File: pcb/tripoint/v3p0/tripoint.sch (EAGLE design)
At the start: 54 parts, among them J1 TC2030-JLINK-NL, J2 TC2030-JLINK-NL, T1 HHM1595A1, U1 STM32F091CC, U2 DW1000, U3 SKY13317, U4 LXDC2HN18A, X1 38.4M, X2 16M

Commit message: added LED, test pads, external signals and Lab11 power symbols
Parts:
- removed J1: TC2030-JLINK-NL, connector:TC2030-JLINK-NL
- added D1: SML-LX0404SIUPGUSB, leds:SML-LX0404SIUPGUSB
- added R5, R6, R7: 1k, passives:RESISTOR0402_RES
- added TP1, TP2: TEST_POINT_0.040IN, headers:TEST_POINT_0.040IN
- added TP3, TP4: TEST-POINT, headers:TEST-POINT
- R1, R2, R3, R4: device rcl:R-EU_R0201 -> passives:RESISTOR0201_RES
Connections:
- net I2C1_SCL renamed EXT_I2C_SCL
- net I2C1_SDA renamed EXT_I2C_SDA
- net SPI_CLK renamed DW_SPI_CLK
- net V1P8 renamed 1V8
- net V1P8_EN renamed REG_EN
- net V3P3 renamed 3V3
- removed net !SPI1_SS: U1.PA4
- removed net !SPI_CS: U2.!SPICS
- removed net GPIO4: J1.VCC, U1.PB10
- removed net GPIO5: J1.GND, U1.PB11
- removed net SPI1_MISO: U1.PA6
- removed net SPI1_MOSI: U1.PA7
- removed net SPI_MISO: U2.SPIMISO
- removed net SPI_MOSI: U2.SPIMOSI
- new net !DW_SPI_CS: U1.PA4, U2.!SPICS
- new net DW_SPI_MISO: U1.PA6, U2.SPIMISO
- new net DW_SPI_MOSI: U1.PA7, U2.SPIMOSI
- new net LED_BLUE: R7.2, U1.PB12
- new net LED_GREEN: R6.2, U1.PB13
- new net LED_RED: R5.2, U1.PB14
- new net N$10: D1.G, R6.1
- new net N$11: D1.B, R7.1
- new net N$12: D1.R, R5.1
- net +3V3: now also D1.VDD
- net GPIO0: now also TP1.TESTPOINT; no longer J1.!RESET
- net GPIO1: now also TP2.TESTPOINT; no longer J1.SWO
- net GPIO2: now also TP3.TESTPOINT, U1.PB10; no longer J1.SWDCLK, U1.PB8
- net GPIO3: now also TP4.TESTPOINT, U1.PB11; no longer J1.SWDIO, U1.PB9
- net INTERRUPT: now also U1.PA2; no longer U1.PA3
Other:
- note added: "EXTERNAL SIGNALS"
- note added: "I2C: Pull-up resistor required"
- note added: "INTERRUPT: used both for waking up from STOP (USART2_TX) and STANDBY (WKUP4)"
- note added: "LED"
- note added: "Note: Additional I2C pull-up resistors required"
- note added: "PC Test Points"
- note added: "Pad Test Points"
- note added: "The following signals must be integrated into all designs using the design block:"

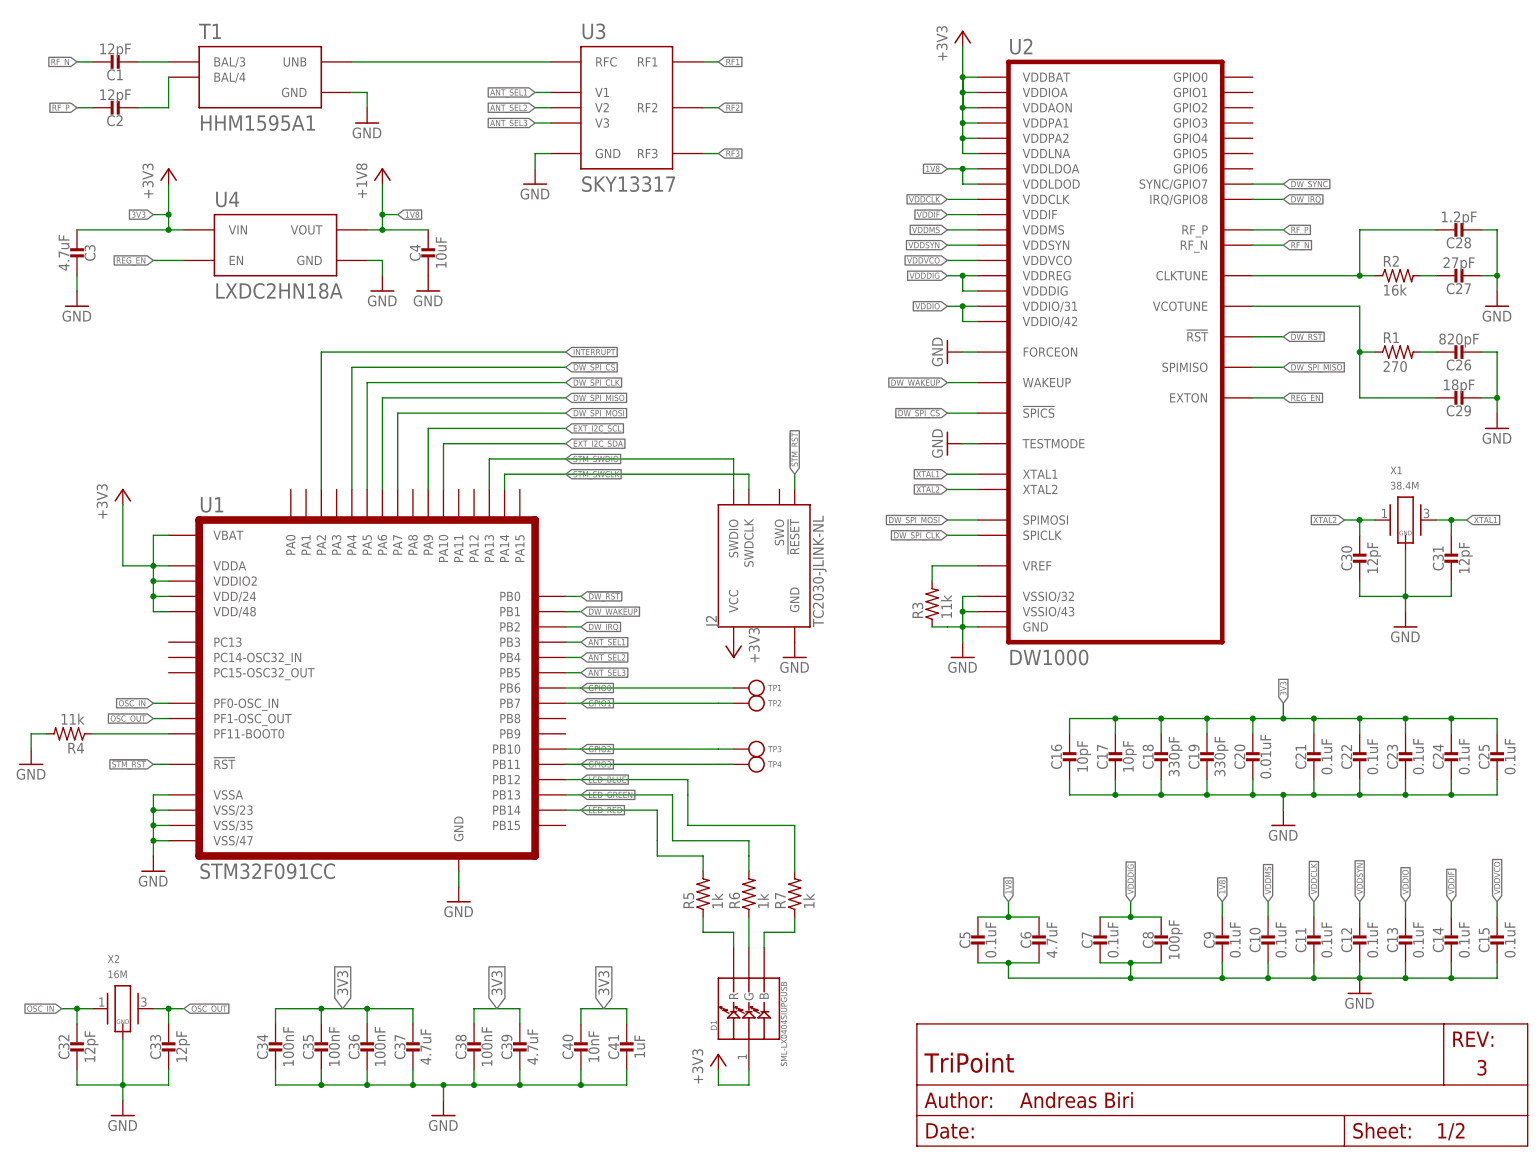
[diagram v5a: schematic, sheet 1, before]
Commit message: corrected decoupling cap values, added correct res for DEEPSLEEP plus missing decoupling caps
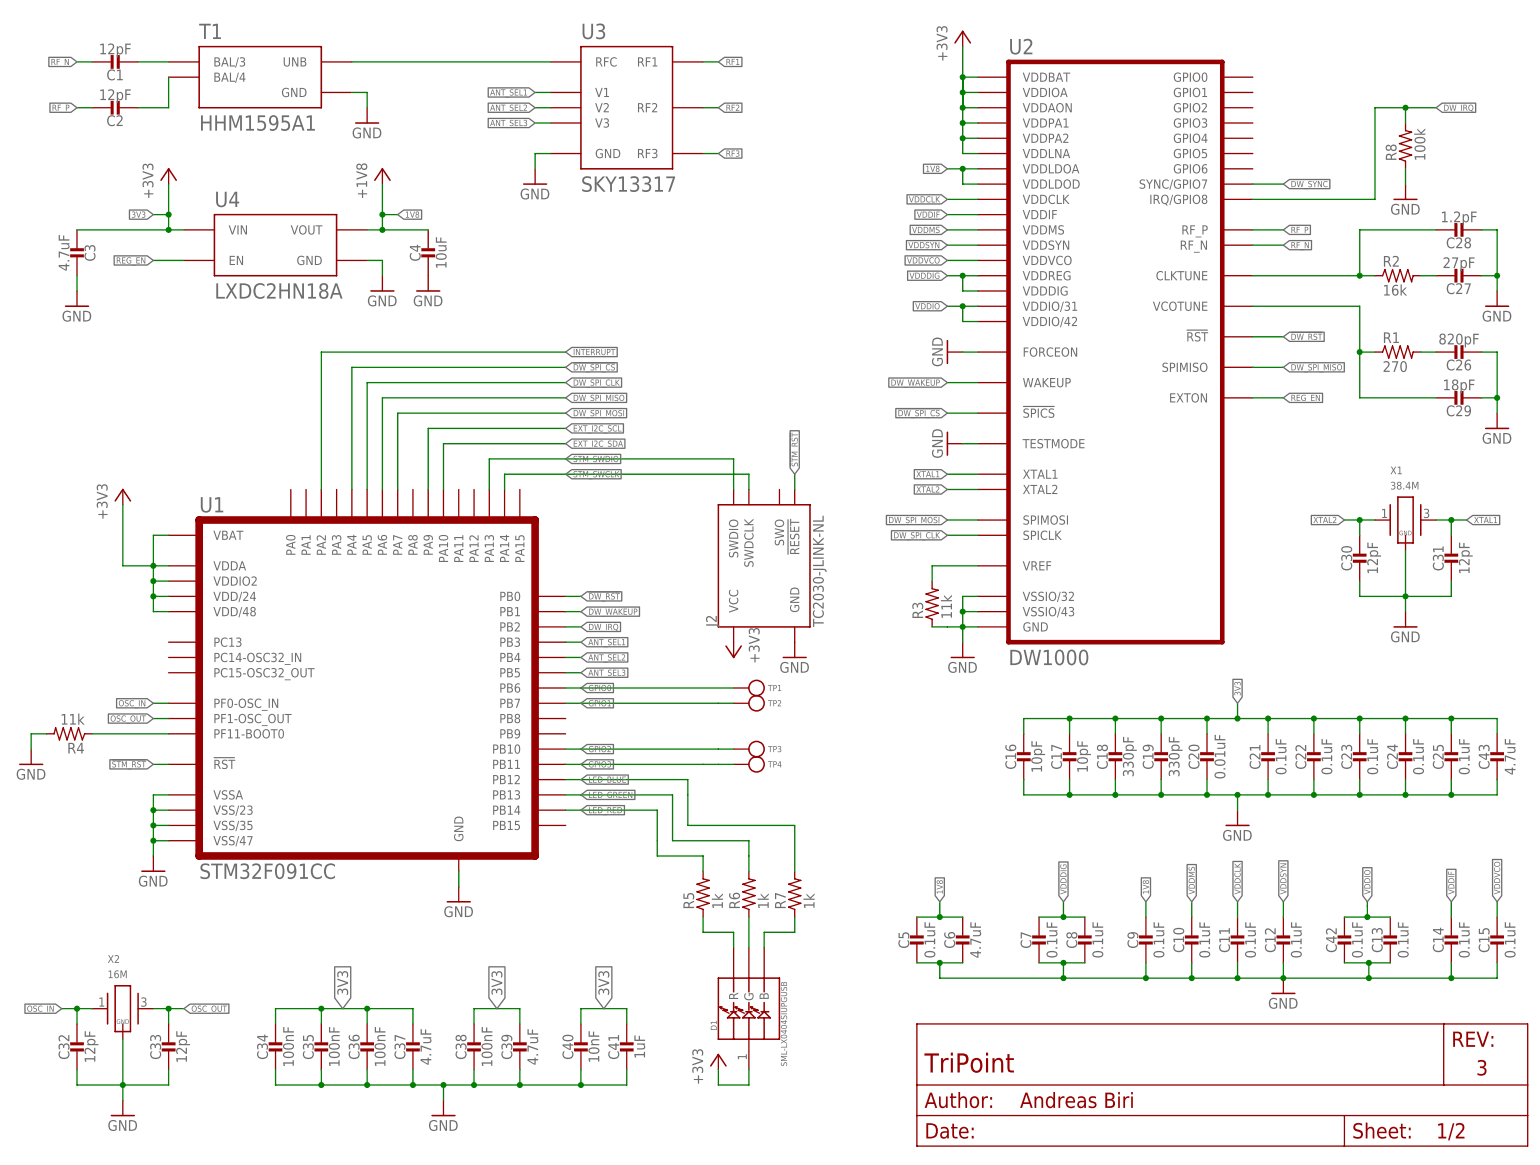
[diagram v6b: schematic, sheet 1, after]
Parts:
- added C42: 0.1uF, passives:CAPACITOR0201_CAP
- added C43: 4.7uF, passives:CAPACITOR0603_CAP
- added R8: 100k, passives:RESISTOR0201_RES
- C8: value 100pF -> 0.1uF
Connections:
- net 3V3: now also C43.1
- net DW_IRQ: now also R8.2
- net GND: now also C42.2, C43.2, R8.1
- net VDDIO: now also C42.1
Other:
- note added: "Pull-down for (DEEP)SLEEP"
- moved on the sheet: C10, C11, C12, C13, C16, C17, C18, C19, C20, C21, C22, C23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

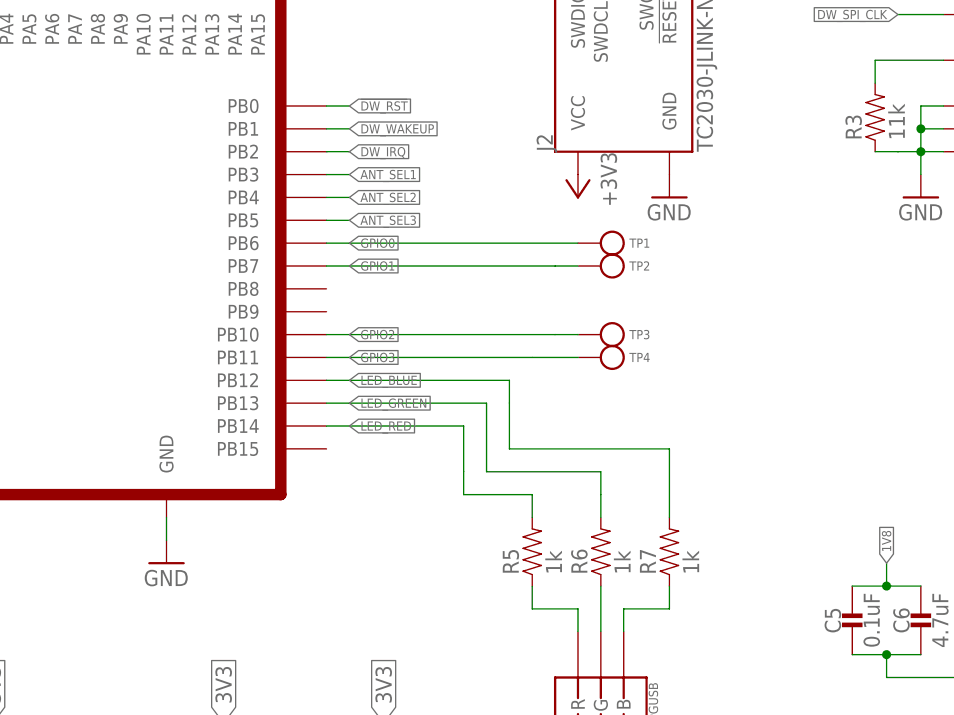
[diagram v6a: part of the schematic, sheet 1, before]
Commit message: completed layout, optimized pin positioning for module
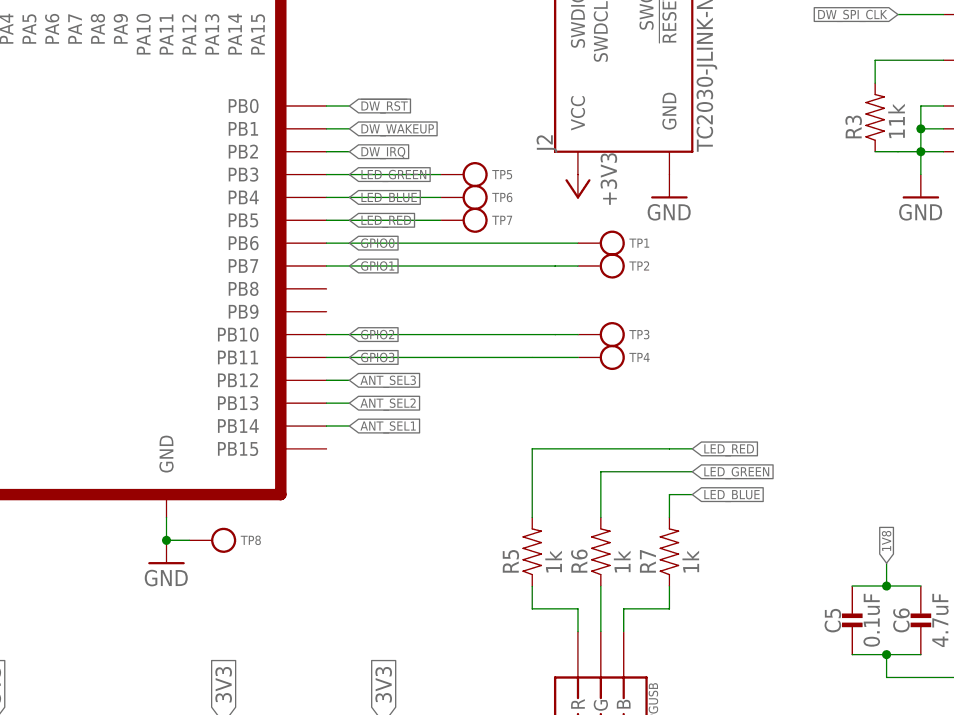
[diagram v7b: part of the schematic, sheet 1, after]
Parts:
- added TP5, TP6, TP7, TP8: TEST-POINT, headers:TEST-POINT
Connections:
- net ANT_SEL1: now also U1.PB14; no longer U1.PB3
- net ANT_SEL2: now also U1.PB13; no longer U1.PB4
- net ANT_SEL3: now also U1.PB12; no longer U1.PB5
- net GND: now also TP8.TESTPOINT
- net LED_BLUE: now also TP6.TESTPOINT, U1.PB4; no longer U1.PB12
- net LED_GREEN: now also TP5.TESTPOINT, U1.PB3; no longer U1.PB13
- net LED_RED: now also TP7.TESTPOINT, U1.PB5; no longer U1.PB14
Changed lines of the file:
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@@
 <part name="C42" library="passives" deviceset="CAPACITOR" device="0201_CAP" value="0.1uF"/>
 <part name="C43" library="passives" deviceset="CAPACITOR" device="0603_CAP" value="4.7uF"/>
+<part name="TP5" library="headers" deviceset="TEST-POINT" device=""/>
+<part name="TP6" library="headers" deviceset="TEST-POINT" device=""/>
+<part name="TP7" library="headers" deviceset="TEST-POINT" device=""/>
+<part name="TP8" library="headers" deviceset="TEST-POINT" device=""/>
 </parts>
 <sheets>
@@
 <instance part="C42" gate="G$1" x="223.52" y="35.56"/>
 <instance part="C43" gate="G$1" x="248.92" y="66.04"/>
+<instance part="TP5" gate="G$1" x="109.22" y="83.82" rot="R180"/>
+<instance part="TP6" gate="G$1" x="109.22" y="81.28" rot="R180"/>
+<instance part="TP7" gate="G$1" x="109.22" y="78.74" rot="R180"/>
+<instance part="TP8" gate="G$1" x="81.28" y="43.18" rot="R180"/>
 </instances>
 <busses>
@@
 <wire x1="76.2" y1="45.72" x2="76.2" y2="43.18" width="0.1524" layer="91"/>
 <pinref part="SUPPLY9" gate="G1" pin="GND"/>
+<pinref part="TP8" gate="G$1" pin="TESTPOINT"/>
+<wire x1="76.2" y1="43.18" x2="78.74" y2="43.18" width="0.1524" layer="91"/>
+<junction x="76.2" y="43.18"/>
 </segment>
 <segment>
@@
 </segment>
 <segment>
-<pinref part="U1" gate="U1" pin="PB3"/>
-<wire x1="93.98" y1="83.82" x2="96.52" y2="83.82" width="0.1524" layer="91"/>
-<label x="96.52" y="83.82" size="1.016" layer="95" xref="yes"/>
+<label x="96.52" y="55.88" size="1.016" layer="95" xref="yes"/>
+<pinref part="U1" gate="U1" pin="PB14"/>
+<wire x1="96.52" y1="55.88" x2="93.98" y2="55.88" width="0.1524" layer="91"/>
 </segment>
 </net>
@@
 </segment>
 <segment>
-<pinref part="U1" gate="U1" pin="PB4"/>
-<wire x1="93.98" y1="81.28" x2="96.52" y2="81.28" width="0.1524" layer="91"/>
-<label x="96.52" y="81.28" size="1.016" layer="95" xref="yes"/>
+<label x="96.52" y="58.42" size="1.016" layer="95" xref="yes"/>
+<pinref part="U1" gate="U1" pin="PB13"/>
+<wire x1="96.52" y1="58.42" x2="93.98" y2="58.42" width="0.1524" layer="91"/>
 </segment>
 </net>
@@
 </segment>
 <segment>
-<pinref part="U1" gate="U1" pin="PB5"/>
-<wire x1="93.98" y1="78.74" x2="96.52" y2="78.74" width="0.1524" layer="91"/>
-<label x="96.52" y="78.74" size="1.016" layer="95" xref="yes"/>
+<pinref part="U1" gate="U1" pin="PB12"/>
+<wire x1="96.52" y1="60.96" x2="93.98" y2="60.96" width="0.1524" layer="91"/>
+<label x="96.52" y="60.96" size="1.016" layer="95" xref="yes"/>
 </segment>
 </net>
@@
 </segment>
 </net>
-<net name="LED_BLUE" class="0">
-<segment>
-<label x="96.52" y="60.96" size="1.016" layer="95" xref="yes"/>
-<wire x1="96.52" y1="60.96" x2="114.3" y2="60.96" width="0.1524" layer="91"/>
-<wire x1="114.3" y1="60.96" x2="114.3" y2="58.42" width="0.1524" layer="91"/>
-<wire x1="114.3" y1="58.42" x2="114.3" y2="53.34" width="0.1524" layer="91"/>
-<wire x1="114.3" y1="53.34" x2="132.08" y2="53.34" width="0.1524" layer="91"/>
-<pinref part="R7" gate="G$1" pin="2"/>
-<wire x1="132.08" y1="53.34" x2="132.08" y2="45.72" width="0.1524" layer="91"/>
-<pinref part="U1" gate="U1" pin="PB12"/>
-<wire x1="96.52" y1="60.96" x2="93.98" y2="60.96" width="0.1524" layer="91"/>
-</segment>
-</net>
-<net name="LED_GREEN" class="0">
-<segment>
-<label x="96.52" y="58.42" size="1.016" layer="95" xref="yes"/>
-<wire x1="96.52" y1="58.42" x2="111.76" y2="58.42" width="0.1524" layer="91"/>
-<wire x1="111.76" y1="58.42" x2="111.76" y2="50.8" width="0.1524" layer="91"/>
-<wire x1="111.76" y1="50.8" x2="124.46" y2="50.8" width="0.1524" layer="91"/>
-<pinref part="R6" gate="G$1" pin="2"/>
-<wire x1="124.46" y1="48.26" x2="124.46" y2="45.72" width="0.1524" layer="91"/>
-<wire x1="124.46" y1="50.8" x2="124.46" y2="48.26" width="0.1524" layer="91"/>
-<pinref part="U1" gate="U1" pin="PB13"/>
-<wire x1="96.52" y1="58.42" x2="93.98" y2="58.42" width="0.1524" layer="91"/>
-</segment>
-</net>
 <net name="INTERRUPT" class="0">
 <segment>
@@
 <pinref part="U1" gate="U1" pin="PA2"/>
 <wire x1="53.34" y1="109.22" x2="53.34" y2="132.08" width="0.1524" layer="91"/>
-</segment>
-</net>
-<net name="LED_RED" class="0">
-<segment>
-<label x="96.52" y="55.88" size="1.016" layer="95" xref="yes"/>
-<pinref part="R5" gate="G$1" pin="2"/>
-<wire x1="116.84" y1="48.26" x2="116.84" y2="45.72" width="0.1524" layer="91"/>
-<wire x1="116.84" y1="48.26" x2="109.22" y2="48.26" width="0.1524" layer="91"/>
-<wire x1="109.22" y1="48.26" x2="109.22" y2="50.8" width="0.1524" layer="91"/>
-<wire x1="109.22" y1="50.8" x2="109.22" y2="55.88" width="0.1524" layer="91"/>
-<pinref part="U1" gate="U1" pin="PB14"/>
-<wire x1="96.52" y1="55.88" x2="93.98" y2="55.88" width="0.1524" layer="91"/>
-<wire x1="109.22" y1="55.88" x2="96.52" y2="55.88" width="0.1524" layer="91"/>
 </segment>
 </net>
@@
 </segment>
 </net>
+<net name="LED_RED" class="0">
+<segment>
+<pinref part="R5" gate="G$1" pin="2"/>
+<wire x1="116.84" y1="45.72" x2="116.84" y2="53.34" width="0.1524" layer="91"/>
+<wire x1="116.84" y1="53.34" x2="132.08" y2="53.34" width="0.1524" layer="91"/>
+<wire x1="132.08" y1="53.34" x2="134.62" y2="53.34" width="0.1524" layer="91"/>
+<label x="134.62" y="53.34" size="1.016" layer="95" xref="yes"/>
+</segment>
+<segment>
+<pinref part="U1" gate="U1" pin="PB5"/>
+<wire x1="93.98" y1="78.74" x2="96.52" y2="78.74" width="0.1524" layer="91"/>
+<label x="96.52" y="78.74" size="1.016" layer="95" xref="yes"/>
+<pinref part="TP7" gate="G$1" pin="TESTPOINT"/>
+<wire x1="96.52" y1="78.74" x2="106.68" y2="78.74" width="0.1524" layer="91"/>
+</segment>
+</net>
+<net name="LED_BLUE" class="0">
+<segment>
+<pinref part="R7" gate="G$1" pin="2"/>
+<wire x1="132.08" y1="45.72" x2="132.08" y2="48.26" width="0.1524" layer="91"/>
+<wire x1="132.08" y1="48.26" x2="134.62" y2="48.26" width="0.1524" layer="91"/>
+<label x="134.62" y="48.26" size="1.016" layer="95" xref="yes"/>
+</segment>
+<segment>
+<pinref part="U1" gate="U1" pin="PB4"/>
+<wire x1="93.98" y1="81.28" x2="96.52" y2="81.28" width="0.1524" layer="91"/>
+<label x="96.52" y="81.28" size="1.016" layer="95" xref="yes"/>
+<pinref part="TP6" gate="G$1" pin="TESTPOINT"/>
+<wire x1="96.52" y1="81.28" x2="106.68" y2="81.28" width="0.1524" layer="91"/>
+</segment>
+</net>
+<net name="LED_GREEN" class="0">
+<segment>
+<pinref part="R6" gate="G$1" pin="2"/>
+<wire x1="124.46" y1="45.72" x2="124.46" y2="50.8" width="0.1524" layer="91"/>
+<wire x1="124.46" y1="50.8" x2="134.62" y2="50.8" width="0.1524" layer="91"/>
+<label x="134.62" y="50.8" size="1.016" layer="95" xref="yes"/>
+</segment>
+<segment>
+<pinref part="U1" gate="U1" pin="PB3"/>
+<wire x1="93.98" y1="83.82" x2="96.52" y2="83.82" width="0.1524" layer="91"/>
+<label x="96.52" y="83.82" size="1.016" layer="95" xref="yes"/>
+<pinref part="TP5" gate="G$1" pin="TESTPOINT"/>
+<wire x1="96.52" y1="83.82" x2="106.68" y2="83.82" width="0.1524" layer="91"/>
+</segment>
+</net>

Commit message: finished routing of TriPoint
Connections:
- net 1V8 renamed +1V8
- removed net 3V3: C16.1, C17.1, C18.1, C19.1, C20.1, C21.1, C22.1, C23.1, C24.1, C25.1, C3.2, C34.1, C35.1, C36.1, C37.1, C38.1, C39.1, C40.1, C41.1, C43.1, U2.VDDAON, U2.VDDBAT, U2.VDDIOA, U2.VDDLNA, U2.VDDPA1, U2.VDDPA2, U4.VIN
- net +3V3: now also C16.1, C17.1, C18.1, C19.1, C20.1, C21.1, C22.1, C23.1, C24.1, C25.1, C3.2, C34.1, C35.1, C36.1, C37.1, C38.1, C39.1, C40.1, C41.1, C43.1, U2.VDDAON, U2.VDDBAT, U2.VDDIOA, U2.VDDLNA, U2.VDDPA1, U2.VDDPA2, U4.VIN
